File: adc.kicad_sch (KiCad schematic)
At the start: 24 parts, among them U70 AD7177-2BRUZ, U75 OPA2189D

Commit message: Schematic complete, maybe
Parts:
- added C768, C770, C776, C777: 10u, Capacitor_SMD:C_0603_1608Metric, symbol Device:C
- added C778: 1u, Capacitor_SMD:C_0402_1005Metric, symbol Device:C
- added L75, L76, L760, L761: 600, Inductor_SMD:L_0603_1608Metric, symbol Parts:L_Ferrite_Power
- added U7: SG-8002CA, Oscillator:Oscillator_SMD_SeikoEpson_SG8002CA-4Pin_7.0x5.0mm, symbol Oscillator:SG-8002CA
- C767, C774, C775: renamed from C?; LCSC (none) -> C52923
- C769, C771: renamed from C?; value 0u1 -> 1u; LCSC (none) -> C52923
- C772, C773: renamed from C?; LCSC (none) -> C307331
- U70: now left out of the parts list
- U75: LCSC (none) -> C881489; now left out of the parts list
- gave numbers to parts that had none: 15
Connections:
- net +2V5: now also L761.1; no longer C771.1, U70.8 (AVDD2)
- net +5VA: now also L760.1; no longer C769.1, U70.7 (AVDD1)
- net GNDPWR: now also U70.23 (AIN2), C768.2, C770.2, C776.2, C777.2, C778.2, U7.2 (GND)
- net +18V5 renamed +18V
- net +3V3: no longer names the net of C774.1, U70.16 (IOVDD)
- net +3V3: now also C776.1, L75.2
- net -3V3 renamed -2V5
- net ADC_CLK renamed 16M
- net 16M: now also U7.3 (OUT)
- net ADC_CS renamed ~{CS}
- net ADC_DIN renamed DIN
- net ADC_DOUT renamed DOUT
- net ADC_SCLK renamed SCLK
- net ADC_SYNC: no longer names the net of U70.15 (~{SYNC}/~{ERROR})
- new net: C768.1, C769.1, L760.2, U70.7 (AVDD1)
- new net: C777.1, C778.1, L76.2, U7.1 (OE), U7.4 (Vcc)
- new net: C770.1, C771.1, L761.2, U70.8 (AVDD2)
- new net +3V3A: L75.1, L76.1
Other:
- note added: "FIXME - osc!"
- note removed: "2V to 5.5V"
- note removed: "FIXME - 3.3A or 3.3D supply?"
- moved on the sheet: C760, C761, C762, C763, C764, C765, C766, C767, C769, C771, C772, C773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

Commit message: Part selection
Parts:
- removed D71, D72: BAT54S, Package_TO_SOT_SMD:SOT-23, symbol Parts:BAT54S
- added D71, D72, D73, D74: 1N5819WS, Diode_SMD:D_SOD-323, symbol Parts:1N5819WS
- C760, C761, C762, C763, C764, C765, C766: footprint Capacitor_SMD:C_0402_1005Metric -> Capacitor_SMD:C_0603_1608Metric; now left out of the parts list
- R760, R761, R763, R764: LCSC (none) -> C25117
- R762, R765: LCSC (none) -> C25104
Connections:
- net +5VA: now also D73.1 (K)
- net GNDPWR: now also D71.1 (K), D72.2 (A), D74.2 (A)
- net at C762.1, C763.1, R761.2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: now also D71.2 (A), D72.1 (K)
- net at C763.2, C766.1, R764.2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: now also D73.2 (A), D74.1 (K)

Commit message: ERC passes.
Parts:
- U7: renamed from U70; footprint RU-24_ADI -> Package_SO:TSSOP-24_4.4x7.8mm_P0.65mm
- U70: renamed from U7; value SG-8002CA -> TG2520SMN-16M-MCG; footprint Oscillator:Oscillator_SMD_SeikoEpson_SG8002CA-4Pin_7.0x5.0mm -> Oscillator:Oscillator_SMD_SeikoEpson_TG2520SMN-xxx-xxxxxx-4Pin_2.5x2.0mm; symbol Oscillator:SG-8002CA -> Oscillator:TG2520SMN-xx.xxxxxxMhz-xxxxNM; now left out of the parts list
- U75: value OPA2189D -> OPA2189DGK; footprint Package_SO:SOIC-8_3.9x4.9mm_P1.27mm -> Package_SO:MSOP-8_3x3mm_P0.65mm; symbol Parts:OPA2189D -> Parts:OPA2189DGK
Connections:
- net at C777.1, C778.1, L76.2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: no longer U70.1 (OE)
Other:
- note removed: "FIXME - osc!"
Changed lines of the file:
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@@
 	(generator_version "9.0")
 	(paper "A4")
-	(text "FIXME - osc!"
-		(exclude_from_sim no)
-		(at 172.72 117.856 0)
-		(effects
-			(font
-				(size 1.27 1.27)
-			)
-		)
-	)
 	(text_box "≈20kΩ input resistance, mitigate by force-sense routing from amplifier."
 		(exclude_from_sim no)
@@
 	)
 	(junction
-		(at 179.07 105.41)
-		(diameter 0)
-		(color 0 0 0 0)
-	)
-	(junction
 		(at 146.05 102.87)
 		(diameter 0)
@@
 	(wire
 		(pts
-			(xy 186.69 105.41) (xy 179.07 105.41)
-		)
-		(stroke
-			(width 0)
-			(type default)
-		)
-	)
-	(wire
-		(pts
 			(xy 219.71 48.26) (xy 214.63 48.26)
 		)
@@
 	(wire
 		(pts
-			(xy 179.07 105.41) (xy 179.07 113.03)
-		)
-		(stroke
-			(width 0)
-			(type default)
-		)
-	)
-	(wire
-		(pts
 			(xy 124.46 88.9) (xy 123.19 88.9)
 		)
@@
 	(wire
 		(pts
-			(xy 179.07 105.41) (xy 175.26 105.41)
+			(xy 175.26 105.41) (xy 186.69 105.41)
 		)
 		(stroke
@@
 	)
 	(symbol
-		(lib_id "Parts:OPA2189D")
+		(lib_id "Parts:OPA2189DGK")
 		(at 106.68 88.9 0)
 		(unit 2)
@@
 			)
 		)
-		(property "Value" "OPA2189D"
+		(property "Value" "OPA2189DGK"
 			(at 112.268 85.344 0)
 			(effects
@@
 			)
 		)
-		(property "Footprint" "Package_SO:SOIC-8_3.9x4.9mm_P1.27mm"
+		(property "Footprint" "Package_SO:MSOP-8_3x3mm_P0.65mm"
 			(at 105.41 88.9 0)
 			(effects
@@
 	)
 	(symbol
-		(lib_id "Parts:OPA2189D")
+		(lib_id "Parts:OPA2189DGK")
 		(at 106.68 60.96 0)
 		(unit 1)
@@
 			)
 		)
-		(property "Value" "OPA2189D"
+		(property "Value" "OPA2189DGK"
 			(at 111.76 56.896 0)
 			(effects
@@
 			)
 		)
-		(property "Footprint" "Package_SO:SOIC-8_3.9x4.9mm_P1.27mm"
+		(property "Footprint" "Package_SO:MSOP-8_3x3mm_P0.65mm"
 			(at 105.41 60.96 0)
 			(effects
@@
 		(on_board yes)
 		(dnp no)
-		(property "Reference" "U70"
+		(property "Reference" "U7"
 			(at 184.15 57.15 0)
 			(effects
@@
 			)
 		)
-		(property "Footprint" "RU-24_ADI"
+		(property "Footprint" "Package_SO:TSSOP-24_4.4x7.8mm_P0.65mm"
 			(at 184.15 81.28 0)
 			(effects
@@
 			(project "lincal"
 				(path "/b054cef4-39e3-49d8-aff0-7ba5a206c187/e69ade03-efa5-476d-a99a-7096b679a0cf"
-					(reference "U70")
+					(reference "U7")
 					(unit 1)
 				)
@@
 	)
 	(symbol
-		(lib_id "Parts:OPA2189D")
+		(lib_id "Parts:OPA2189DGK")
 		(at 146.05 110.49 0)
 		(mirror y)
@@
 			)
 		)
-		(property "Value" "OPA2189D"
+		(property "Value" "OPA2189DGK"
 			(at 145.796 110.744 0)
 			(effects
@@
 			)
 		)
-		(property "Footprint" "Package_SO:SOIC-8_3.9x4.9mm_P1.27mm"
+		(property "Footprint" "Package_SO:MSOP-8_3x3mm_P0.65mm"
 			(at 147.32 110.49 0)
 			(effects
@@
 	)
 	(symbol
-		(lib_id "Oscillator:SG-8002CA")
+		(lib_id "Oscillator:TG2520SMN-xx.xxxxxxMhz-xxxxNM")
 		(at 186.69 113.03 0)
 		(unit 1)
 		(exclude_from_sim no)
-		(in_bom yes)
+		(in_bom no)
 		(on_board yes)
 		(dnp no)
-		(property "Reference" "U7"
+		(property "Reference" "U70"
 			(at 181.864 109.22 0)
 			(effects
@@
 			)
 		)
-		(property "Value" "SG-8002CA"
-			(at 187.96 119.38 0)
+		(property "Value" "TG2520SMN-16M-MCG"
+			(at 186.944 119.634 0)
 			(effects
 				(font
@@
 			)
 		)
-		(property "Footprint" "Oscillator:Oscillator_SMD_SeikoEpson_SG8002CA-4Pin_7.0x5.0mm"
+		(property "Footprint" "Oscillator:Oscillator_SMD_SeikoEpson_TG2520SMN-xxx-xxxxxx-4Pin_2.5x2.0mm"
 			(at 204.47 121.92 0)
 			(effects
@@
 			)
 		)
-		(property "Datasheet" "https://support.epson.biz/td/api/doc_check.php?mode=dl&lang=en&Parts=SG-8002DC"
+		(property "Datasheet" "https://support.epson.biz/td/api/doc_check.php?dl=app_TG2520SMN&lang=en"
 			(at 184.15 113.03 0)
 			(effects
@@
 			)
 		)
-		(property "Description" "CMOS Clock Oscillator 1 to 125 MHz"
+		(property "Description" "Crystal Oscillator Low Profile / High Stability TCXO"
 			(at 186.69 113.03 0)
 			(effects
@@
 			(project ""
 				(path "/b054cef4-39e3-49d8-aff0-7ba5a206c187/e69ade03-efa5-476d-a99a-7096b679a0cf"
-					(reference "U7")
+					(reference "U70")
 					(unit 1)
 				)

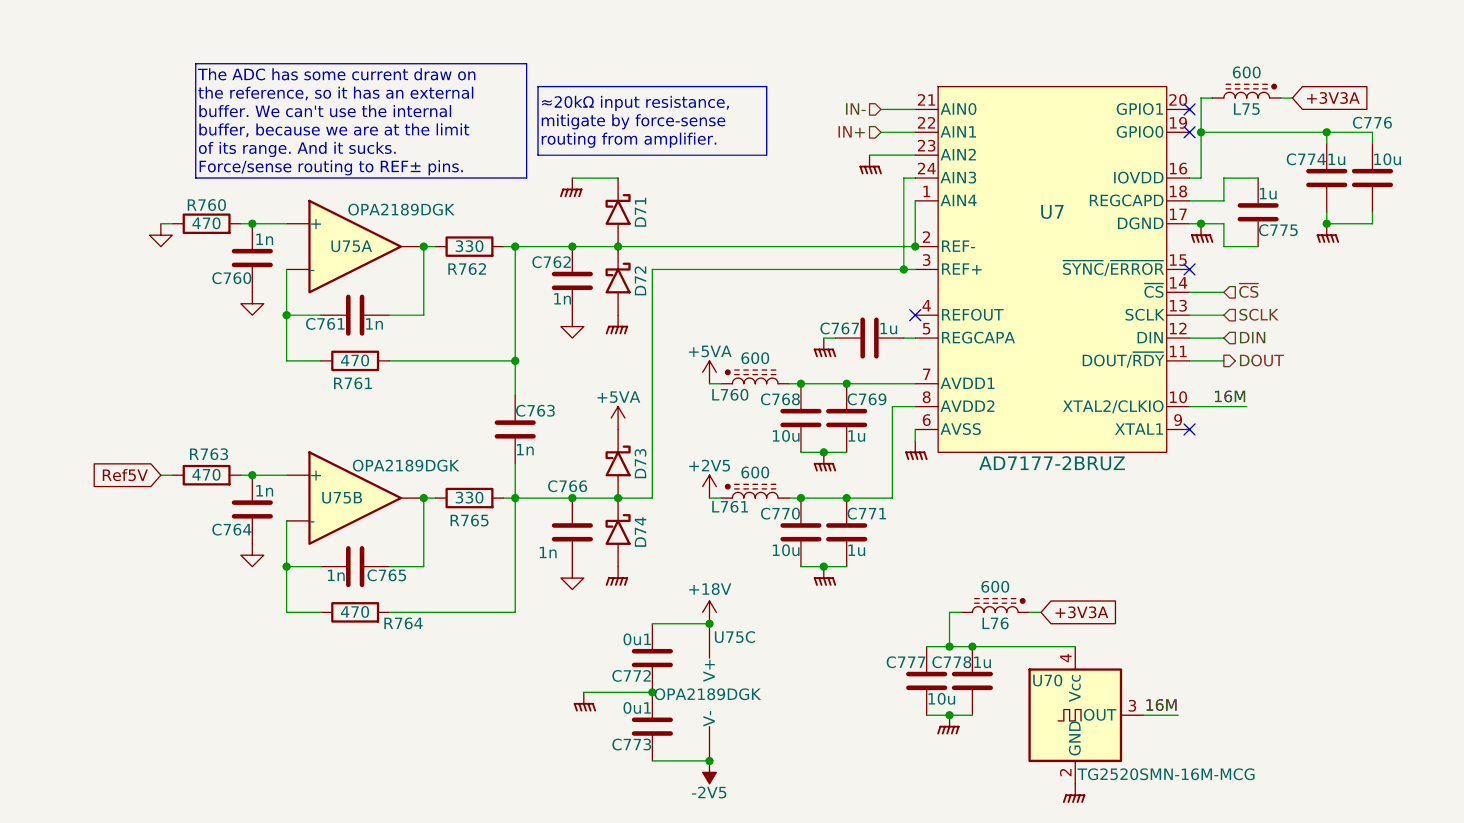
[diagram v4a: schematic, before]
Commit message: Layout underway
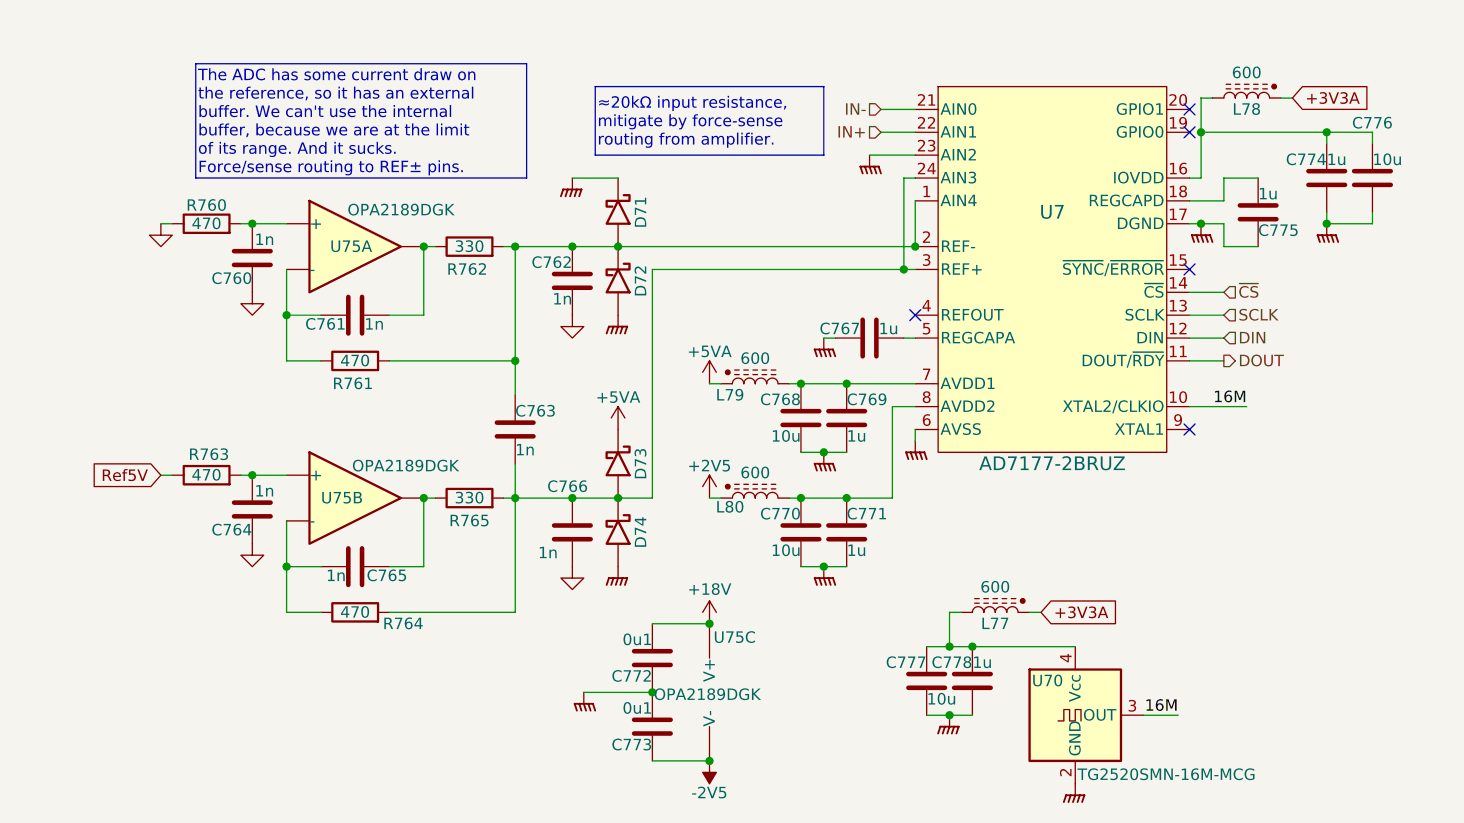
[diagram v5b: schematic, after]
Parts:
- renumbered L76 to L77, L75 to L78, L760 to L79, L761 to L80
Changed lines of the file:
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@@
 	(text_box "≈20kΩ input resistance, mitigate by force-sense routing from amplifier."
 		(exclude_from_sim no)
-		(at 127 43.18 0)
+		(at 133.35 43.18 0)
 		(size 25.4 7.62)
 		(margins 0.254 0.254 0.254 0.254)
@@
 		(on_board yes)
 		(dnp no)
-		(property "Reference" "L76"
+		(property "Reference" "L77"
 			(at 177.8 102.87 90)
 			(effects
@@
 			(project "lincal"
 				(path "/b054cef4-39e3-49d8-aff0-7ba5a206c187/e69ade03-efa5-476d-a99a-7096b679a0cf"
-					(reference "L76")
+					(reference "L77")
 					(unit 1)
 				)
@@
 		(on_board yes)
 		(dnp no)
-		(property "Reference" "L761"
+		(property "Reference" "L80"
 			(at 148.336 89.916 90)
 			(effects
@@
 			(project "lincal"
 				(path "/b054cef4-39e3-49d8-aff0-7ba5a206c187/e69ade03-efa5-476d-a99a-7096b679a0cf"
-					(reference "L761")
+					(reference "L80")
 					(unit 1)
 				)
@@
 		(on_board yes)
 		(dnp no)
-		(property "Reference" "L75"
+		(property "Reference" "L78"
 			(at 205.74 45.72 90)
 			(effects
@@
 			(project "lincal"
 				(path "/b054cef4-39e3-49d8-aff0-7ba5a206c187/e69ade03-efa5-476d-a99a-7096b679a0cf"
-					(reference "L75")
+					(reference "L78")
 					(unit 1)
 				)
@@
 		(on_board yes)
 		(dnp no)
-		(property "Reference" "L760"
+		(property "Reference" "L79"
 			(at 148.336 77.47 90)
 			(effects
@@
 			(project "lincal"
 				(path "/b054cef4-39e3-49d8-aff0-7ba5a206c187/e69ade03-efa5-476d-a99a-7096b679a0cf"
-					(reference "L760")
+					(reference "L79")
 					(unit 1)
 				)

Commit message: Whew.  DACs routed
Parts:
- U75: footprint Package_SO:MSOP-8_3x3mm_P0.65mm -> Parts:OPA2189
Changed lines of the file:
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@@
 			)
 		)
-		(property "Footprint" "Package_SO:MSOP-8_3x3mm_P0.65mm"
+		(property "Footprint" "Parts:OPA2189"
 			(at 105.41 88.9 0)
 			(effects
@@
 			)
 		)
-		(property "Footprint" "Package_SO:MSOP-8_3x3mm_P0.65mm"
+		(property "Footprint" "Parts:OPA2189"
 			(at 105.41 60.96 0)
 			(effects
@@
 			)
 		)
-		(property "Footprint" "Package_SO:MSOP-8_3x3mm_P0.65mm"
+		(property "Footprint" "Parts:OPA2189"
 			(at 147.32 110.49 0)
 			(effects

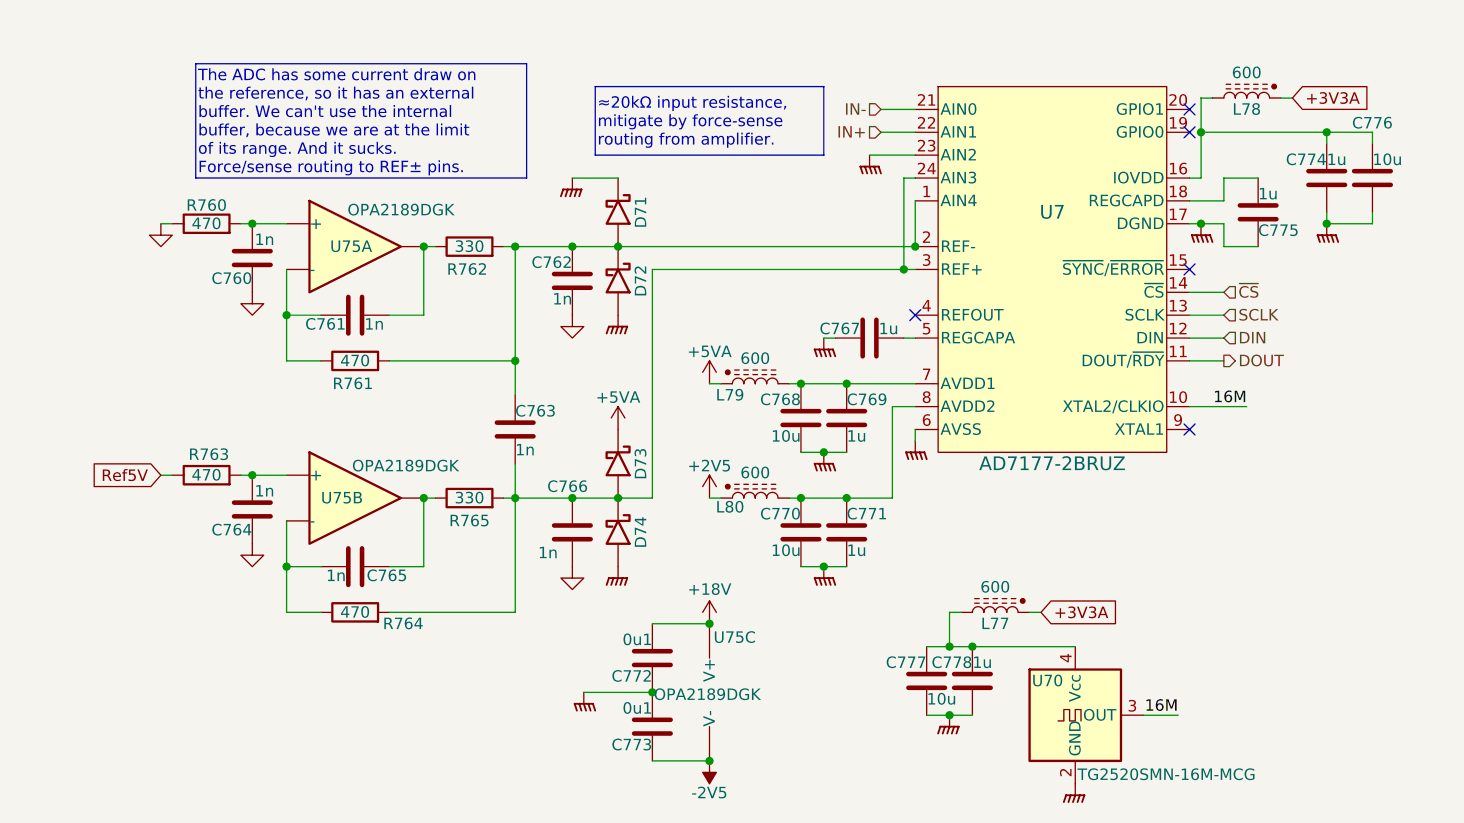
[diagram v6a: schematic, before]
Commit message: Tweaks following spice simulation.
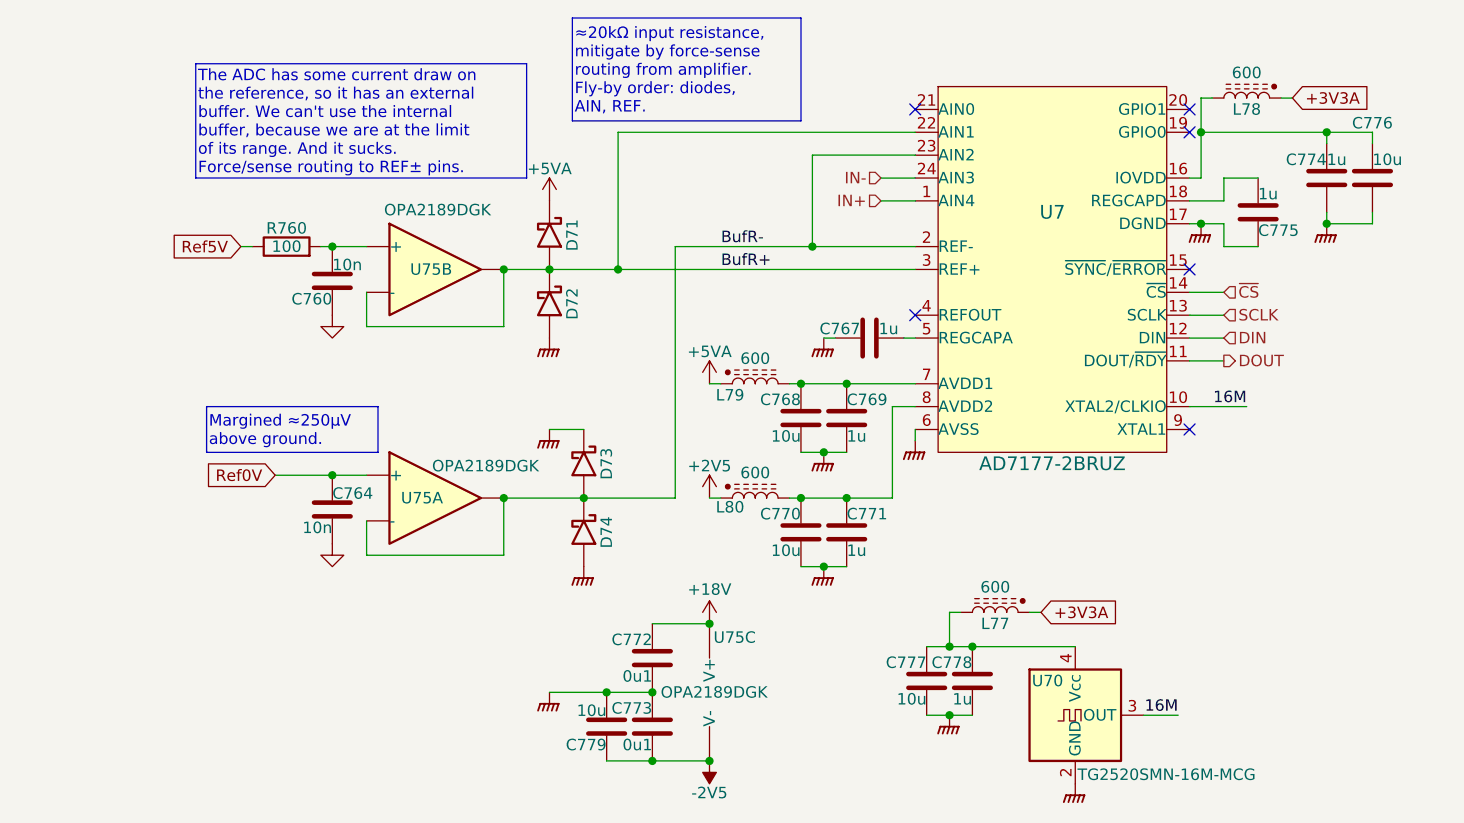
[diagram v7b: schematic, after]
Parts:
- removed C761, C762, C763, C765, C766: 1n, Capacitor_SMD:C_0603_1608Metric, symbol Device:C
- removed R761, R763, R764: 470, Resistor_SMD:R_0402_1005Metric, symbol Device:R
- removed R762, R765: 330, Resistor_SMD:R_0402_1005Metric, symbol Device:R
- added C779: 10u, Capacitor_SMD:C_0603_1608Metric, symbol Device:C
- C760, C764: value 1n -> 10n; LCSC (none) -> C307500; now in the parts list
- R760: value 470 -> 100; LCSC C25117 -> (none)
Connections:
- net +18V: now also C772.1; no longer C772.2
- net +5VA: now also D71.1 (K); no longer D73.1 (K)
- net -2V5: now also C773.2, C779.2; no longer C773.1
- net GND: no longer R760.1
- net GNDPWR: now also C772.2, C773.1, D73.1 (K), C779.1; no longer C772.1, C773.2, D71.1 (K), U7.23 (AIN2)
- net IN+: now also U7.1 (AIN4); no longer U7.22 (AIN1)
- net IN-: now also U7.24 (AIN3); no longer U7.21 (AIN0)
- net Ref5V: now also R760.1
- net BufR-: now reaches D73.2 (A), D74.1 (K)
- net BufR-: now also U7.2 (REF-), U7.23 (AIN2), U75.1, U75.2 (-); no longer U7.24 (AIN3), U7.3 (REF+)
- net Ref0V: now reaches C764.1
- net Ref0V: now also U75.3 (+); no longer U75.5 (+)
- net at C760.1, R760.2: now also U75.5 (+); no longer U75.3 (+)
- net BufR+: now reaches D71.2 (A), D72.1 (K)
- net BufR+: now also U7.22 (AIN1), U7.3 (REF+), U75.6 (-), U75.7; no longer U7.1 (AIN4), U7.2 (REF-)
- no-connect marks 5 -> 6
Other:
- moved on the sheet: C760, C764, C772, C773, D71, D72, D73, D74, R760, U75A, U75B

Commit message: About to delete scan...
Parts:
- added C761, C764: 330p, Capacitor_SMD:C_0603_1608Metric, symbol Device:C
- added C762, C765: 10n, Capacitor_SMD:C_0603_1608Metric, symbol Device:C
- added R761, R763: 10, Resistor_SMD:R_0402_1005Metric, symbol Device:R
- added R762, R764: 330, Resistor_SMD:R_0402_1005Metric, symbol Device:R
- R760: LCSC (none) -> C25076
- U7: Stock (none) -> 1
- U70: footprint Oscillator:Oscillator_SMD_SeikoEpson_TG2520SMN-xxx-xxxxxx-4Pin_2.5x2.0mm -> Parts:TG2520SMN
- U75: Stock (none) -> 15
- renumbered C764 to C763
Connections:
- net BufR+: now also C762.1, R761.2, R762.2; no longer U75.6 (-), U75.7
- net BufR-: now also C765.1, R763.2, R764.2; no longer U75.1, U75.2 (-)
- net GND: now also C762.2, C765.2
- new net: C764.1, R763.1, U75.1
- new net: C764.2, R764.1, U75.2 (-)
- new net: C761.2, R762.1, U75.6 (-)
- new net: C761.1, R761.1, U75.7
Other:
- moved on the sheet: C760, C763, D71, D72, D73, D74, R760, U75A, U75B
